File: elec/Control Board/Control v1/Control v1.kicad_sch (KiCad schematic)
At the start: 19 parts, among them J1 Conn_02x12_Odd_Even, J14 Conn_01x08, J15 Conn_01x08, J16 Conn_01x08, J17 Conn_01x08, J18 Conn_01x08, J19 Conn_02x18_Odd_Even, J20 Conn_01x10_MountingPin, J4 Screw_Terminal_01x02, J5 Screw_Terminal_01x02, J7 DB9_Female_MountingHoles, SW1 SW_DIP_x08

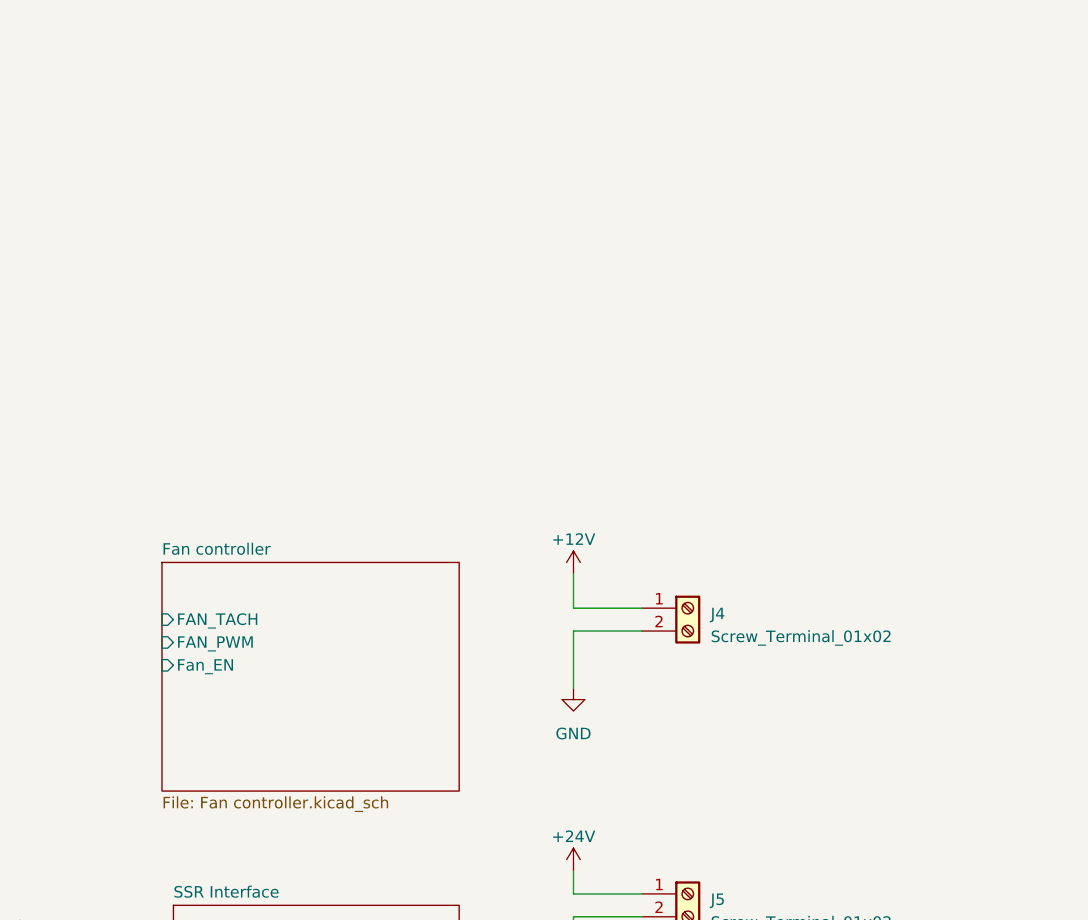
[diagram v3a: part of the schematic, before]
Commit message: Switch to FAN POWER.
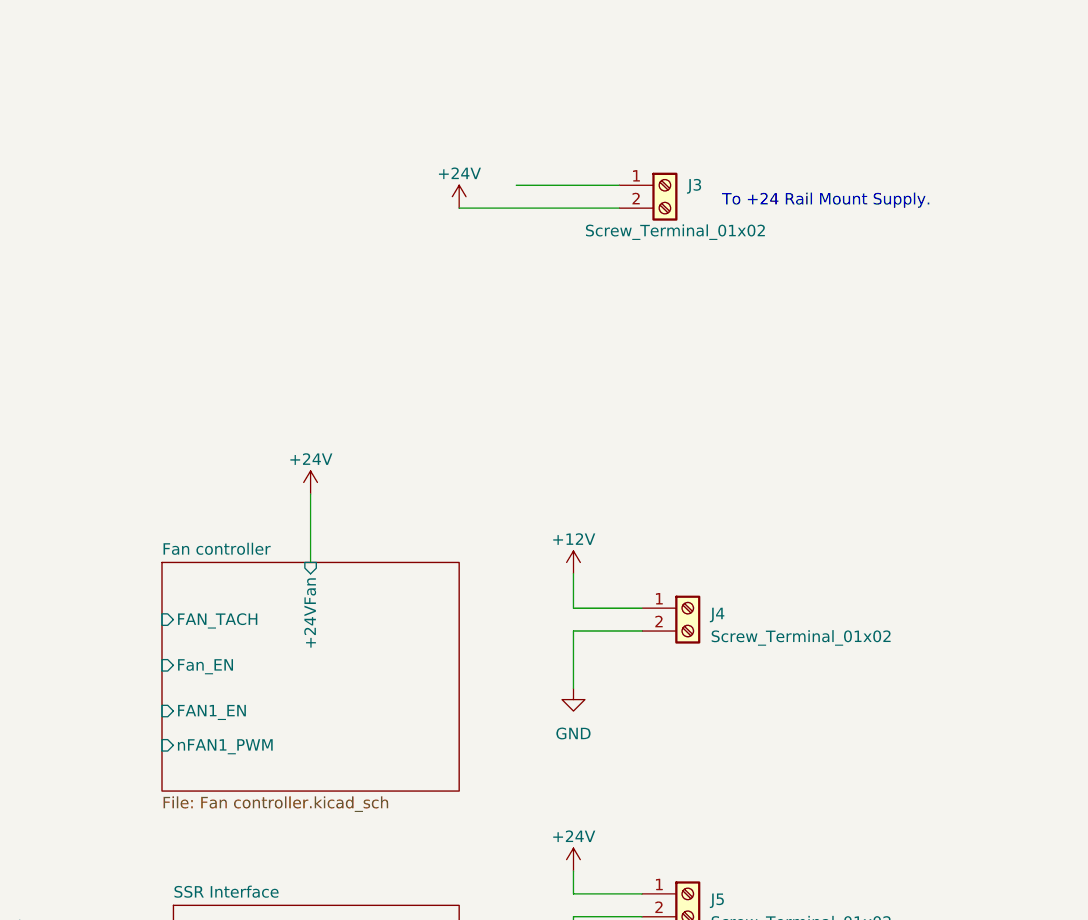
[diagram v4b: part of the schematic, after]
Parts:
- added J3: Screw_Terminal_01x02, TerminalBlock_MetzConnect:TerminalBlock_MetzConnect_Type073_RT02602HBLU_1x02_P5.08mm_Horizontal, symbol Connector:Screw_Terminal_01x02
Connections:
- net +24V: now also J3.2 (Pin_2)
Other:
- sheet Fan controller ports: added +24VFan, FAN1_EN, nFAN1_PWM; removed FAN_PWM
- note added: "To +24 Rail Mount Supply."
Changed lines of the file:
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@@
     (stroke (width 0) (type default))
   )
+  (wire (pts (xy 353.06 181.61) (xy 353.06 189.23))
+    (stroke (width 0) (type default))
+  )
   (wire (pts (xy 152.4 130.81) (xy 177.8 130.81))
     (stroke (width 0) (type default))
@@
     (stroke (width 0) (type default))
   )
+  (wire (pts (xy 369.57 149.86) (xy 387.35 149.86))
+    (stroke (width 0) (type default))
+  )
   (wire (pts (xy 152.4 138.43) (xy 158.75 138.43))
     (stroke (width 0) (type default))
@@
     (stroke (width 0) (type default))
   )
+  (wire (pts (xy 375.92 147.32) (xy 387.35 147.32))
+    (stroke (width 0) (type default))
+  )
   (wire (pts (xy 243.84 74.93) (xy 264.16 74.93))
     (stroke (width 0) (type default))
@@
     )
   )
+  (text "To +24 Rail Mount Supply." (at 398.78 149.86 0)
+    (effects (font (size 1.27 1.27)) (justify left bottom))
+  )
   (text "Thermocouple block" (at 34.29 144.78 0)
     (effects (font (size 1.27 1.27)) (justify left bottom))
@@
     )
   )
+  (symbol (lib_id "power:+24V") (at 353.06 181.61 0) (unit 1)
+    (in_bom yes) (on_board yes) (dnp no) (fields_autoplaced)
+    (property "Reference" "#PWR04" (at 353.06 185.42 0)
+      (effects (font (size 1.27 1.27)) hide)
+    )
+    (property "Value" "+24V" (at 353.06 177.8 0)
+      (effects (font (size 1.27 1.27)))
+    )
+    (property "Footprint" "" (at 353.06 181.61 0)
+      (effects (font (size 1.27 1.27)) hide)
+    )
+    (property "Datasheet" "" (at 353.06 181.61 0)
+      (effects (font (size 1.27 1.27)) hide)
+    )
+    (pin "1")
+    (instances
+      (project "Control v1"
+        (path "/c68c9deb-8d4d-42f0-adf8-4d3022f4ee59"
+          (reference "#PWR04") (unit 1)
+        )
+      )
+    )
+  )
   (symbol (lib_id "power:+12V") (at 123.19 52.07 0) (unit 1)
     (in_bom yes) (on_board yes) (dnp no) (fields_autoplaced)
@@
     )
   )
+  (symbol (lib_id "Connector:Screw_Terminal_01x02") (at 392.43 147.32 0) (unit 1)
+    (in_bom yes) (on_board yes) (dnp no)
+    (property "Reference" "J3" (at 394.97 147.3199 0)
+      (effects (font (size 1.27 1.27)) (justify left))
+    )
+    (property "Value" "Screw_Terminal_01x02" (at 383.54 152.4 0)
+      (effects (font (size 1.27 1.27)) (justify left))
+    )
+    (property "Footprint" "TerminalBlock_MetzConnect:TerminalBlock_MetzConnect_Type073_RT02602HBLU_1x02_P5.08mm_Horizontal" (at 392.43 147.32 0)
+      (effects (font (size 1.27 1.27)) hide)
+    )
+    (property "Datasheet" "~" (at 392.43 147.32 0)
+      (effects (font (size 1.27 1.27)) hide)
+    )
+    (pin "1")
+    (pin "2")
+    (instances
+      (project "Control v1"
+        (path "/c68c9deb-8d4d-42f0-adf8-4d3022f4ee59"
+          (reference "J3") (unit 1)
+        )
+        (path "/c68c9deb-8d4d-42f0-adf8-4d3022f4ee59/0cb2f0dc-fe38-451d-b752-5d12a98f8d03"
+          (reference "J8") (unit 1)
+        )
+      )
+    )
+  )
   (symbol (lib_id "Connector_Generic:Conn_01x08") (at 154.94 113.03 0) (mirror y) (unit 1)
     (in_bom yes) (on_board yes) (dnp no)
@@
     )
   )
+  (symbol (lib_id "power:+24V") (at 369.57 149.86 0) (mirror y) (unit 1)
+    (in_bom yes) (on_board yes) (dnp no) (fields_autoplaced)
+    (property "Reference" "#PWR02" (at 369.57 153.67 0)
+      (effects (font (size 1.27 1.27)) hide)
+    )
+    (property "Value" "+24V" (at 369.57 146.05 0)
+      (effects (font (size 1.27 1.27)))
+    )
+    (property "Footprint" "" (at 369.57 149.86 0)
+      (effects (font (size 1.27 1.27)) hide)
+    )
+    (property "Datasheet" "" (at 369.57 149.86 0)
+      (effects (font (size 1.27 1.27)) hide)
+    )
+    (pin "1")
+    (instances
+      (project "Control v1"
+        (path "/c68c9deb-8d4d-42f0-adf8-4d3022f4ee59/0cb2f0dc-fe38-451d-b752-5d12a98f8d03"
+          (reference "#PWR02") (unit 1)
+        )
+        (path "/c68c9deb-8d4d-42f0-adf8-4d3022f4ee59"
+          (reference "#PWR03") (unit 1)
+        )
+      )
+    )
+  )
   (symbol (lib_id "power:GND") (at 382.27 203.2 0) (unit 1)
     (in_bom yes) (on_board yes) (dnp no) (fields_autoplaced)
@@
       (effects (font (size 1.27 1.27)) (justify left))
     )
-    (pin "FAN_PWM" input (at 336.55 198.12 180)
+    (pin "Fan_EN" input (at 336.55 200.66 180)
+      (effects (font (size 1.27 1.27)) (justify left))
+    )
+    (pin "+24VFan" input (at 353.06 189.23 90)
+      (effects (font (size 1.27 1.27)) (justify right))
+    )
+    (pin "nFAN1_PWM" input (at 336.55 209.55 180)
       (effects (font (size 1.27 1.27)) (justify left))
     )
-    (pin "Fan_EN" input (at 336.55 200.66 180)
+    (pin "FAN1_EN" input (at 336.55 205.74 180)
       (effects (font (size 1.27 1.27)) (justify left))
     )

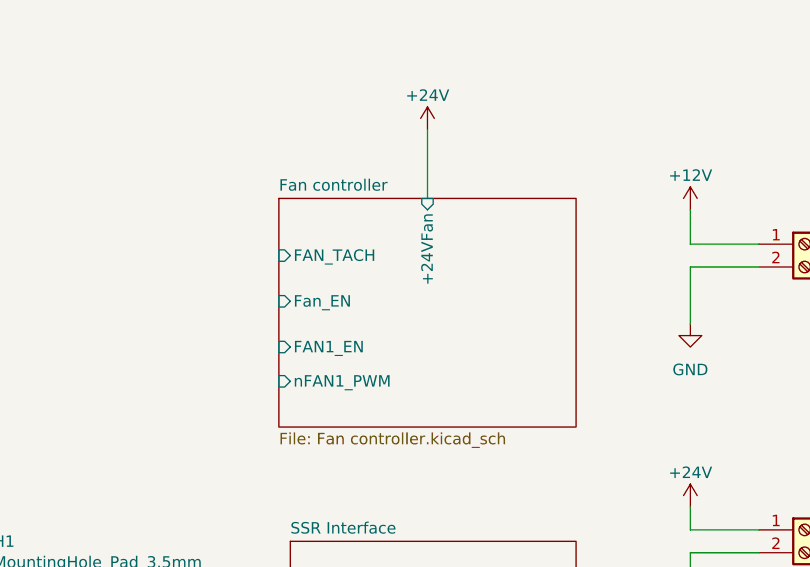
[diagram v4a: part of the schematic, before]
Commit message: Complete Fan1 PWM control. Fan1 Tach / FG.
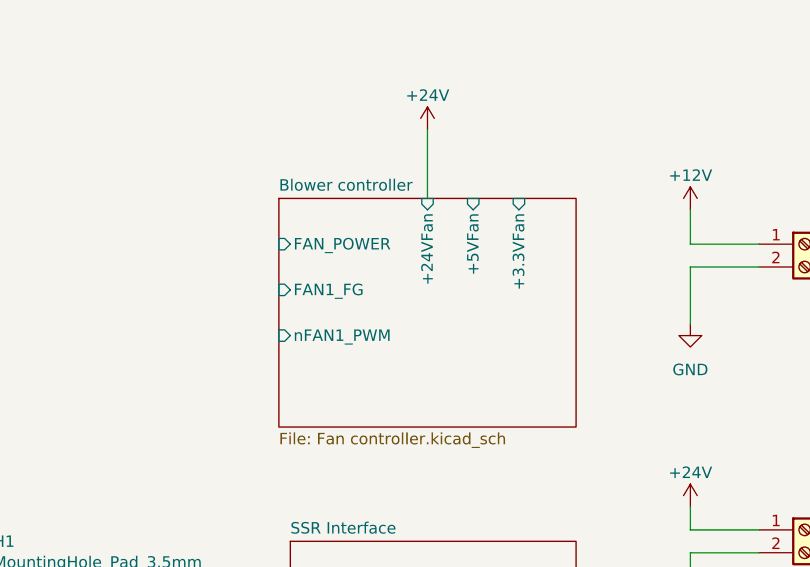
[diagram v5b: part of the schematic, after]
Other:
- sheet Fan controller renamed Blower controller
- sheet Blower controller ports: added +3.3VFan, +5VFan, FAN1_FG, FAN_POWER; removed FAN1_EN, FAN_TACH, Fan_EN
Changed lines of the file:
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@@
     (stroke (width 0.1524) (type solid))
     (fill (color 0 0 0 0.0000))
-    (property "Sheetname" "Fan controller" (at 336.55 188.5184 0)
+    (property "Sheetname" "Blower controller" (at 336.55 188.5184 0)
       (effects (font (size 1.27 1.27)) (justify left bottom))
     )
@@
       (effects (font (size 1.27 1.27)) (justify left top))
     )
-    (pin "FAN_TACH" input (at 336.55 195.58 180)
-      (effects (font (size 1.27 1.27)) (justify left))
-    )
-    (pin "Fan_EN" input (at 336.55 200.66 180)
-      (effects (font (size 1.27 1.27)) (justify left))
-    )
     (pin "+24VFan" input (at 353.06 189.23 90)
       (effects (font (size 1.27 1.27)) (justify right))
     )
-    (pin "nFAN1_PWM" input (at 336.55 209.55 180)
+    (pin "nFAN1_PWM" input (at 336.55 204.47 180)
       (effects (font (size 1.27 1.27)) (justify left))
     )
-    (pin "FAN1_EN" input (at 336.55 205.74 180)
+    (pin "+5VFan" input (at 358.14 189.23 90)
+      (effects (font (size 1.27 1.27)) (justify right))
+    )
+    (pin "FAN1_FG" input (at 336.55 199.39 180)
       (effects (font (size 1.27 1.27)) (justify left))
     )
+    (pin "+3.3VFan" input (at 363.22 189.23 90)
+      (effects (font (size 1.27 1.27)) (justify right))
+    )
+    (pin "FAN_POWER" input (at 336.55 194.31 180)
+      (effects (font (size 1.27 1.27)) (justify left))
+    )

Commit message: Add fan circuits. Add thermocouple interface circuits.
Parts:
- added F1 (x2): Polyfuse 6A, GeneralPurposeAlarmDevicePCB:PlaceHolderOpossum, symbol Device:Polyfuse
- added J22: Conn_01x05_Socket, symbol Connector:Conn_01x05_Socket
- added J8: Screw_Terminal_01x02, symbol Connector:Screw_Terminal_01x02
- added R301 (x3): 1R, Resistor_SMD:R_0603_1608Metric_Pad0.98x0.95mm_HandSolder, symbol Device:R
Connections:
- net Thermocouple Amplifier with 1-Wire Breakout Board - MAX31850K/A0: now also J22.3 (Pin_3)
- net Thermocouple Amplifier with 1-Wire Breakout Board - MAX31850K/A1: now also J22.1 (Pin_1)
- net Thermocouple Amplifier with 1-Wire Breakout Board - MAX31850K/A2: now also J22.2 (Pin_2)
- net Thermocouple Amplifier with 1-Wire Breakout Board - MAX31850K/A3: now also J22.4 (Pin_4)
- net BLOWER_PWM: now also R301.2
- net BLOWER_TACH: now also R301.2
- net Blower controller/FAN1_FG: now also R301.1
- net Blower controller/FAN_POWER: now also R301.1
- net Blower controller/nFAN1_PWM: now also R301.1
- new net BLOWER_????: R301.2
- new net SSR Interface/Heater_SSR_High: J8.1 (Pin_1)
- new net SSR Interface/Heater_SSR_Low: J8.2 (Pin_2)
- new net Thermocouple Amplifier with 1-Wire Breakout Board - MAX31850K/+3.3V_MAX31850K: J22.5 (Pin_5)
- no-connect marks 1 -> 3
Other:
- sheet Adafruit-MAX31850-thermocouple renamed Thermocouple Amplifier with 1-Wire Breakout Board - MAX31850K
- sheet Adafruit-MAX31855-thermocouple renamed Thermocouple Amplifier 3wire Interface breakout board - MAX31855 
- sheet Adafruit-MAX31856 renamed Thermocouple Amplifier SPI breakout board - MAX31865
- sheet SSR Interface ports: added +5V_SSR, Heater_SSR_High, Heater_SSR_Low; removed Heater_SSR
- sheet Thermocouple Amplifier 3wire Interface breakout board - MAX31855  ports: added +3.3V_MAX31855, +5V_MAX31855; removed none
- sheet Thermocouple Amplifier SPI breakout board - MAX31865 ports: added +3.3V_MAX31856, +5V_MAX31856; removed none
- sheet Thermocouple Amplifier with 1-Wire Breakout Board - MAX31850K ports: added +3.3V_MAX31850K, +5V_MAX31850K; removed none
- note added: "Blower Controller Signals FAN_POWER the Due output sets high to enable power to the blower. FAN1_FG is the Due input gets tachometer signal. Two low going edeges per revoluion. nFan1_PWM is negative aserted PWM to control blower speed."
- note added: "One Wire Thermocouple amplifiter and Interface DATA is bidorectional on the Due GPIO"
- note added: "Power in from where? +24 +12 +5"
- note added: "SSR Interface (Solid State Relay) HEATER the Due output sets high to switch AC power to enable preheaters Heater_SSR_High passes +5V through to the SSR. Heater_SSR_High goes low, conducts, to turn on SSR when HEATER is asserted high."
- note added: "THERMOCOUPLE BLOCK"
- note added: "To SSR control."
- note removed: "Thermocouple block"
- moved on the sheet: H1, H2, H3, H4, H5

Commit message: Move some components for rough placement.
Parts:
- removed F1 (x2): Polyfuse 6A, GeneralPurposeAlarmDevicePCB:PlaceHolderOpossum, symbol Device:Polyfuse
- removed J22: Conn_01x05_Socket, symbol Connector:Conn_01x05_Socket
- removed J3: Screw_Terminal_01x02, TerminalBlock_MetzConnect:TerminalBlock_MetzConnect_Type073_RT02602HBLU_1x02_P5.08mm_Horizontal, symbol Connector:Screw_Terminal_01x02
- removed SW1: SW_DIP_x08, PubInv_PCB:SMDIP-16_L11.39_W6.7mm, symbol Switch:SW_DIP_x08
- added R101 (x2): 1R0, Resistor_SMD:R_0603_1608Metric_Pad0.98x0.95mm_HandSolder, symbol Device:R
- renumbered J1 to J10, J4 to J12, J5 to J13, J8 to J14, J7 to J2, J14 to J3, J15 to J4, J16 to J5, J17 to J6, J18 to J7, J19 to J8, J20 to J9
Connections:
- net BLOWER_???? is gone; now on net BLOWER_ENABLE: R301.2
- net SCL: now also R101.1; no longer J10.20 (Pin_20)
- net SDA: now also R101.2; no longer J10.19 (Pin_19)
- net D32: now reaches A1.D32, J8.13 (Pin_13)
- net BLOWER_ENABLE: now reaches A1.D22, J8.3 (Pin_3)
- new net: J10.20 (Pin_20), R101.2
- new net: J10.19 (Pin_19), R101.1
- no-connect marks 3 -> 9
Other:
- sheet SSR Interface ports: added +24V_SSR; removed +5V_SSR
- note added: "Due pin 22"
- note added: "To Flow Metter(s)"
- note added: "To chassis mounted +24V."
- note added: "nCS_GPAD"
- note removed: "Power in from where? +24 +12 +5"
- note removed: "To +24 Rail Mount Supply."

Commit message: commit of test change.
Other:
- note added: "A change."
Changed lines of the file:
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@@
     (effects (font (size 0.635 0.635)) (justify left bottom))
+  )
+  (text "A change." (at 365.76 125.73 0)
+    (effects (font (size 1.27 1.27)) (justify left bottom))
   )
   (text "To chassis mounted +24V." (at 403.86 224.79 0)
